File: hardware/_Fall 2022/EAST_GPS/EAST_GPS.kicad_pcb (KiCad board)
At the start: 2 copper layers, 76.2 x 66.7 mm, 7 parts, among them J1 Conn_02x09_Odd_Even, U1 GPS-14414, U2 RFM69HCW_Breakout

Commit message: EAST JLC files
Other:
- board text added: "Ari Bobesh Charlie Babe Jiayuan Liu Lili Baker Rowan Jansens"
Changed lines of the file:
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@@
       (outputformat 1)
       (mirror false)
-      (drillshape 1)
+      (drillshape 0)
       (scaleselection 1)
-      (outputdirectory "")
+      (outputdirectory "JLC/")
     )
   )
@@
   (gr_line (start 117.949638 129.540466) (end 168.3512 129.540466) (layer "Edge.Cuts") (width 0.2))
   (gr_arc (start 117.949638 129.540466) (mid 143.150419 62.848534) (end 168.3512 129.540466) (layer "Edge.Cuts") (width 0.2))
+  (gr_text "Ari Bobesh\nCharlie Babe\nJiayuan Liu\nLili Baker\nRowan Jansens" (at 143.002 96.0628) (layer "B.SilkS")
+    (effects (font (size 2 2) (thickness 0.15)) (justify mirror))
+  )
   (segment (start 130.4848 115.6512) (end 129.6416 114.808) (width 0.508) (layer "F.Cu") (net 1))
   (segment (start 119.4 110.6878) (end 121.6914 112.9792) (width 0.508) (layer "F.Cu") (net 1))

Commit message: pcb fixes
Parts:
- U1: moved to B.Cu
- moved U1 0.27 mm to (158.4, 97.5), turned to 0 degrees
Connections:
- U2 pad 4: unconnected-(U2-Pad4) -> /RX 2
- U2 pad 6: /MOSI 1 -> /MISO 1
- U2 pad 7: /MISO 1 -> /MOSI 1
- U2 pad 9: unconnected-(U2-Pad9) -> /TX 2
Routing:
- net /RX 2: track 0.00 -> 18.4 mm
- net /SDA 2: track 8.59 -> 24.2 mm
- net /TX 2: track 0.00 -> 9.54 mm
- net /SCL 2: track 8.59 -> 17.8 mm
- net /GND: track 13.3 -> 6.81 mm, vias 3 -> 2
- net /MISO 1: track 15.7 -> 19.9 mm
- net /SCK 1: track 35.9 -> 37.6 mm
- net /3.3V: track 50.1 -> 49.4 mm
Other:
- board text added: "3.3"
- board text added: "CS1"
- board text added: "CS2"
- board text added: "CS3"
- board text added: "CS4"
- board text added: "GND"
- board text added: "MISO"
- board text added: "MOSI"
- board text added: "RX1"
- board text added: "RX2"
- board text added: "SCK"
- board text added: "SCL1"
- board text added: "SCL2"
- board text added: "SDA1"
- board text added: "SDA2"
- board text added: "TX1"
- board text added: "TX2"
- board text added: "VBAT"

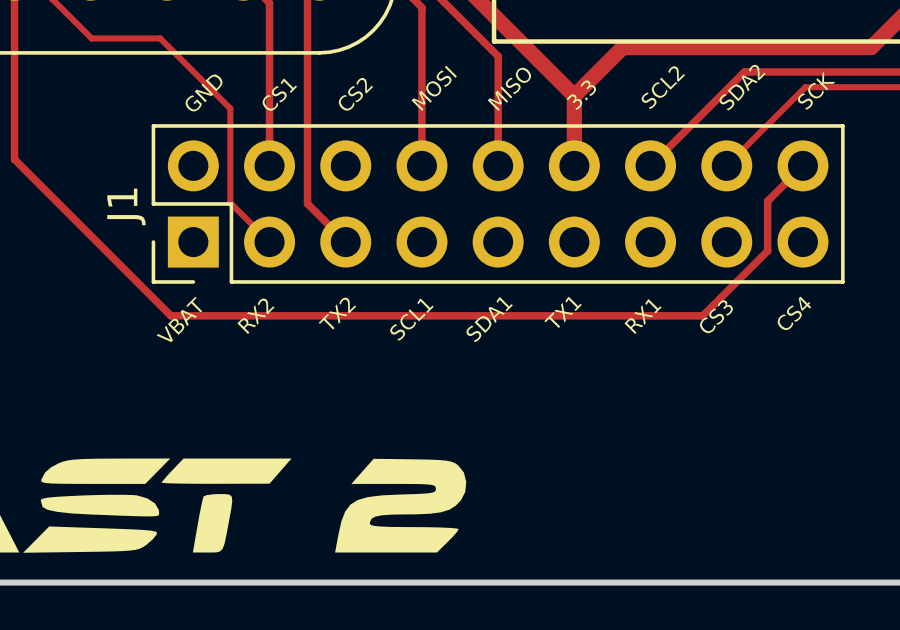
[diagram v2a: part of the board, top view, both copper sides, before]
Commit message: fixed a few pcb silkscreen things
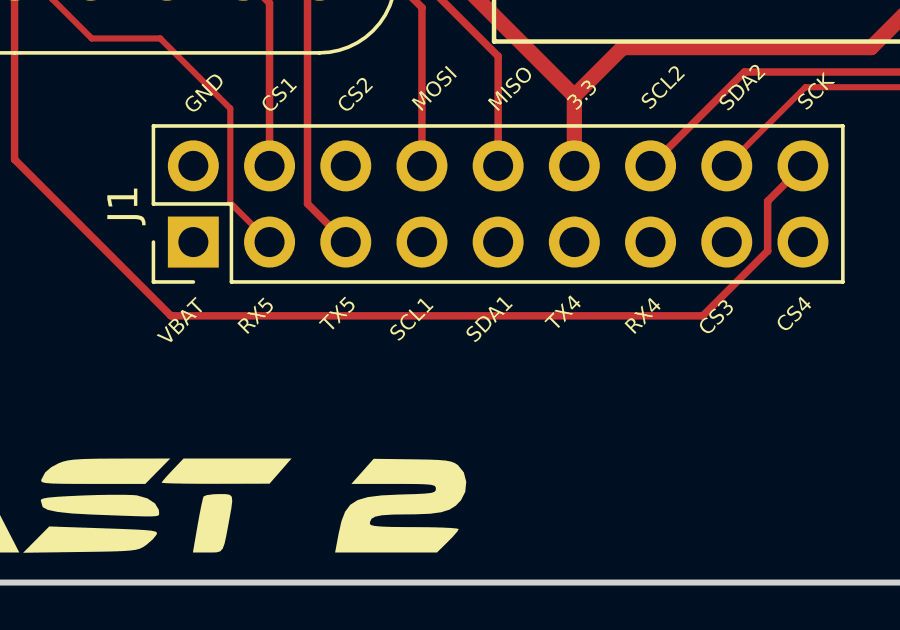
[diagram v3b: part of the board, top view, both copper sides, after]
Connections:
- net /MISO 1 renamed /MISO
- net /MOSI 1 renamed /MOSI
- net /RX 1 renamed /RX 4
- net /RX 2 renamed /RX 5
- net /SCK 1 renamed /SCK
- net /TX 1 renamed /TX 4
- net /TX 2 renamed /TX 5
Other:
- board text added: "RX4"
- board text added: "RX5"
- board text added: "TX4"
- board text added: "TX5"
- board text removed: "RX1"
- board text removed: "RX2"
- board text removed: "TX1"
- board text removed: "TX2"

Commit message: pcb ship version
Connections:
- U1 pad 4: /SDA 2 -> /SDA 1
- U1 pad 5: /SCL 2 -> /SCL 1
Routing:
- net /SCL 1: track 0.00 -> 33.7 mm, vias 0 -> 2
- net /SDA 1: track 0.00 -> 28.3 mm, vias 0 -> 2
- net /SDA 2: track 24.2 -> 0.00 mm
- net /SCL 2: track 17.8 -> 0.00 mm
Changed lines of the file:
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@@
       (net 2 "/3.3V") (pinfunction "3.3V") (pintype "power_in") (solder_mask_margin 0.1016))
     (pad "4" thru_hole circle (at 2.413 11.557 270) (size 1.8796 1.8796) (drill 1.016) (layers *.Cu *.Mask)
-      (net 13 "/SDA 2") (pinfunction "SDA") (pintype "output") (solder_mask_margin 0.1016))
+      (net 15 "/SDA 1") (pinfunction "SDA") (pintype "output") (solder_mask_margin 0.1016))
     (pad "5" thru_hole circle (at 4.953 11.557 270) (size 1.8796 1.8796) (drill 1.016) (layers *.Cu *.Mask)
-      (net 14 "/SCL 2") (pinfunction "SCL") (pintype "output") (solder_mask_margin 0.1016))
+      (net 16 "/SCL 1") (pinfunction "SCL") (pintype "output") (solder_mask_margin 0.1016))
     (pad "6" thru_hole circle (at -5.207 -11.303 270) (size 1.8796 1.8796) (drill 1.016) (layers *.Cu *.Mask)
       (net 24 "unconnected-(U1-Pad6)") (pinfunction "WAKE") (pintype "input+no_connect") (solder_mask_margin 0.1016))
@@
   (segment (start 152.124 118.487901) (end 149.961901 120.65) (width 0.25) (layer "F.Cu") (net 12))
   (segment (start 149.961901 120.65) (end 132.2324 120.65) (width 0.25) (layer "F.Cu") (net 12))
-  (segment (start 165.1 108.330014) (end 164.059586 107.2896) (width 0.2032) (layer "F.Cu") (net 13))
-  (segment (start 162.7124 113.03) (end 165.1 110.6424) (width 0.2032) (layer "F.Cu") (net 13))
-  (segment (start 164.059586 107.2896) (end 162.5323 107.2896) (width 0.2032) (layer "F.Cu") (net 13))
-  (segment (start 150.759 115.6512) (end 153.3802 113.03) (width 0.2032) (layer "F.Cu") (net 13))
-  (segment (start 162.5323 107.2896) (end 160.782 109.0399) (width 0.2032) (layer "F.Cu") (net 13))
-  (segment (start 165.1 110.6424) (end 165.1 108.330014) (width 0.2032) (layer "F.Cu") (net 13))
-  (segment (start 153.3802 113.03) (end 162.7124 113.03) (width 0.2032) (layer "F.Cu") (net 13))
-  (segment (start 159.8399 112.522) (end 163.322 109.0399) (width 0.25) (layer "F.Cu") (net 14))
-  (segment (start 151.3482 112.522) (end 159.8399 112.522) (width 0.25) (layer "F.Cu") (net 14))
-  (segment (start 148.219 115.6512) (end 151.3482 112.522) (width 0.25) (layer "F.Cu") (net 14))
+  (segment (start 143.139 118.1912) (end 143.139 119.4662) (width 0.25) (layer "F.Cu") (net 15))
+  (segment (start 160.782 114.9604) (end 160.782 109.0399) (width 0.25) (layer "F.Cu") (net 15))
+  (segment (start 154.3679 121.3745) (end 160.782 114.9604) (width 0.25) (layer "F.Cu") (net 15))
+  (segment (start 145.0848 121.3745) (end 154.3679 121.3745) (width 0.25) (layer "F.Cu") (net 15))
+  (segment (start 143.139 119.4662) (end 143.2052 119.5324) (width 0.25) (layer "F.Cu") (net 15))
+  (via (at 143.2052 119.5324) (size 0.8) (drill 0.4) (layers "F.Cu" "B.Cu") (net 15))
+  (via (at 145.0848 121.3745) (size 0.8) (drill 0.4) (layers "F.Cu" "B.Cu") (net 15))
+  (segment (start 145.0473 121.3745) (end 145.0848 121.3745) (width 0.25) (layer "B.Cu") (net 15))
+  (segment (start 143.2052 119.5324) (end 145.0473 121.3745) (width 0.25) (layer "B.Cu") (net 15))
+  (segment (start 142.3416 121.666) (end 142.7988 122.1232) (width 0.25) (layer "F.Cu") (net 16))
+  (segment (start 140.599 119.7202) (end 140.6652 119.7864) (width 0.25) (layer "F.Cu") (net 16))
+  (segment (start 163.322 114.0968) (end 163.322 109.0399) (width 0.25) (layer "F.Cu") (net 16))
+  (segment (start 155.2956 122.1232) (end 163.322 114.0968) (width 0.25) (layer "F.Cu") (net 16))
+  (segment (start 142.7988 122.1232) (end 155.2956 122.1232) (width 0.25) (layer "F.Cu") (net 16))
+  (segment (start 140.599 118.1912) (end 140.599 119.7202) (width 0.25) (layer "F.Cu") (net 16))
+  (via (at 142.3416 121.666) (size 0.8) (drill 0.4) (layers "F.Cu" "B.Cu") (net 16))
+  (via (at 140.6652 119.7864) (size 0.8) (drill 0.4) (layers "F.Cu" "B.Cu") (net 16))
+  (segment (start 140.6652 119.7864) (end 142.3416 121.4628) (width 0.25) (layer "B.Cu") (net 16))
+  (segment (start 142.3416 121.4628) (end 142.3416 121.666) (width 0.25) (layer "B.Cu") (net 16))
   (zone (net 1) (net_name "/GND") (layer "B.Cu") (hatch edge 0.508)
     (connect_pads (clearance 1))
